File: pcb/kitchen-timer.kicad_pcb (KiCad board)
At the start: 2 copper layers, 41 x 33 mm, 23 parts, among them IC1 ArduinoProMini, J1 EX, J2 3.3V, J3 RT, J4 Conn_01x03, J5 Conn_01x03, J6 LCD, Q1 BC337, Q2 BC327, Q3 BC337, Q4 BC327, Q5 BC337

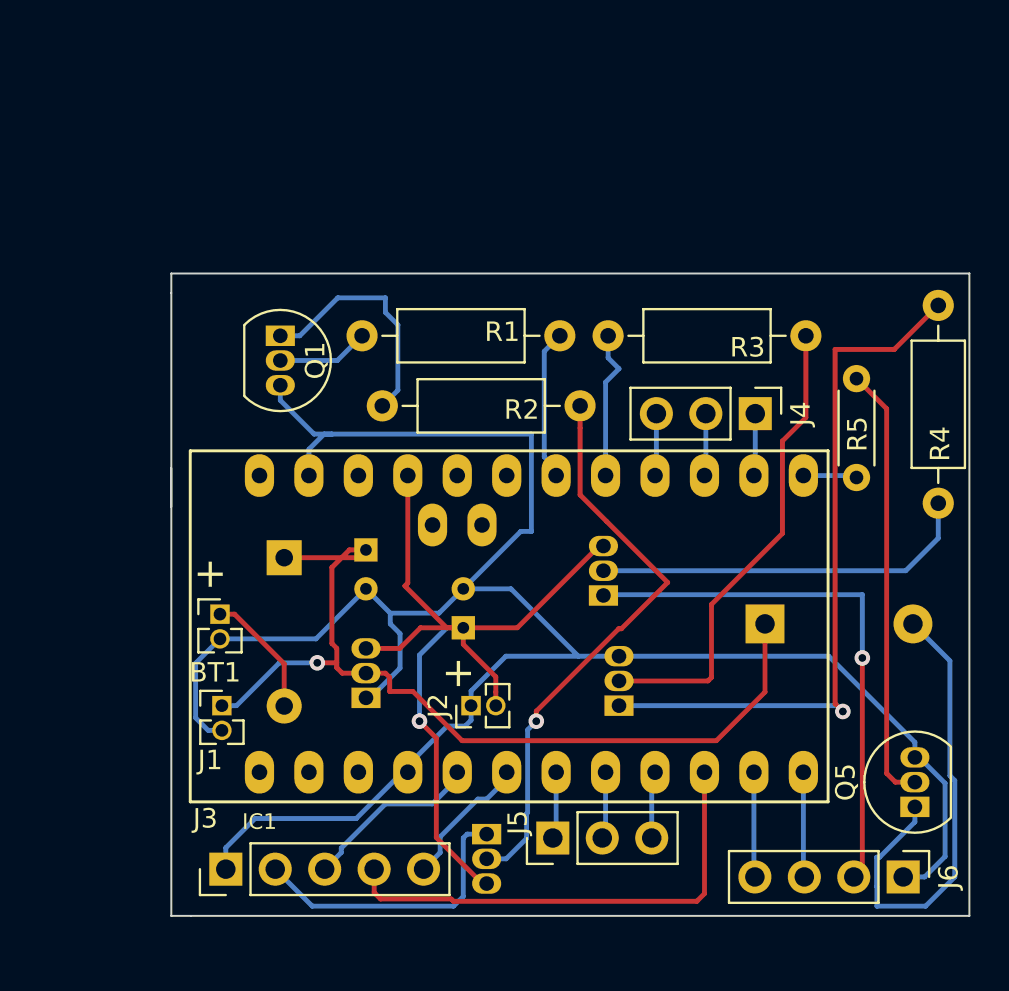
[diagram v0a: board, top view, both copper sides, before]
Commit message: added gnd plane on back
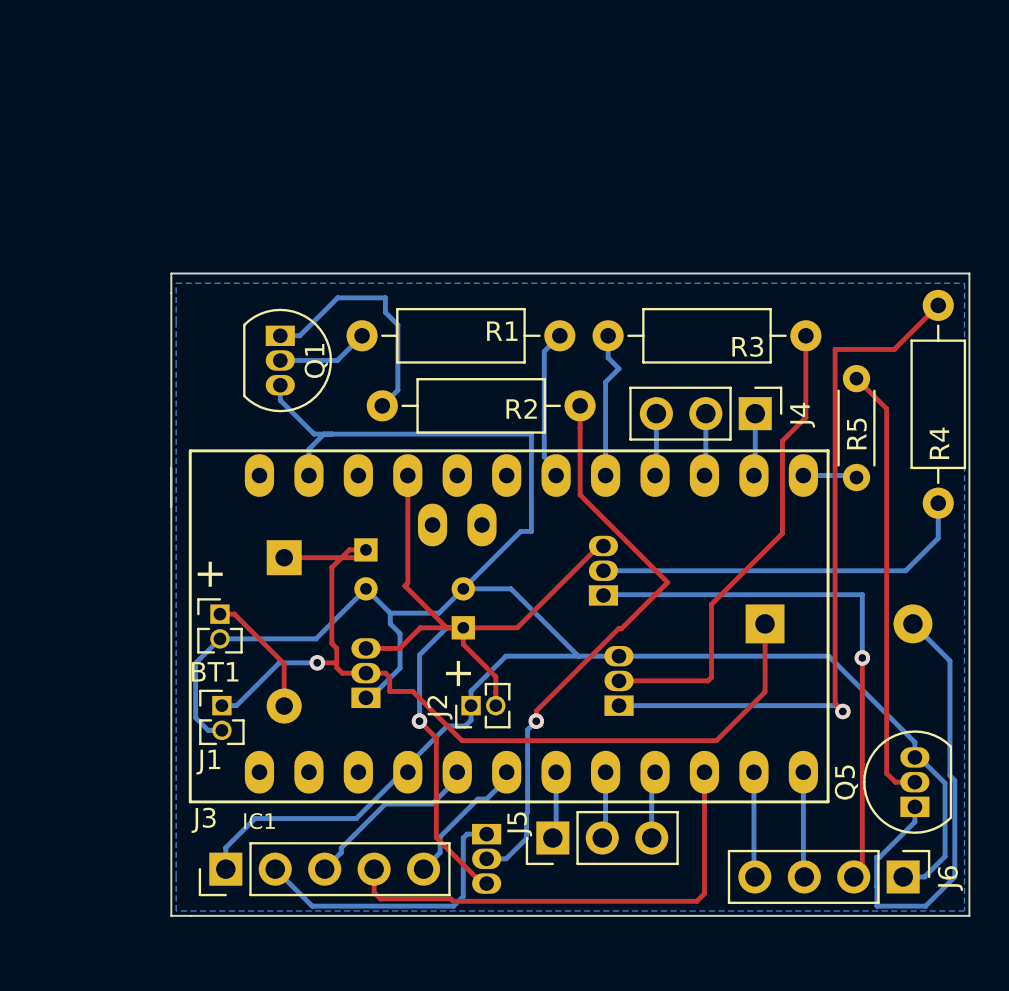
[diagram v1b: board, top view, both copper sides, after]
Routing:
- added copper zone on B.Cu, net -BATT
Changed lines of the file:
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@@
     (pad_drill 0.6)
     (pad_to_mask_clearance 0)
+    (solder_mask_min_width 0.25)
     (aux_axis_origin 0 0)
     (visible_elements FFFFFF7F)
@@
       (outputformat 1)
       (mirror false)
-      (drillshape 1)
+      (drillshape 0)
       (scaleselection 1)
-      (outputdirectory ""))
+      (outputdirectory "/tmp/"))
   )
   (net 0 "")
@@
   (segment (start 149.75 78.95) (end 148.2 77.4) (width 0.25) (layer F.Cu) (net 37))
   (segment (start 149.75 97.68) (end 149.75 78.95) (width 0.25) (layer F.Cu) (net 37))
+  (zone (net 1) (net_name -BATT) (layer B.Cu) (hatch edge 0.508)
+    (connect_pads (clearance 0.508))
+    (min_thickness 0.254)
+    (fill yes (arc_segments 16) (thermal_gap 0.508) (thermal_bridge_width 0.508))
+    (polygon
+      (pts
+        (xy 113.25 72.5) (xy 153.75 72.5) (xy 153.75 104.75) (xy 113.25 104.75) (xy 113.25 103)
+        (xy 113.25 76.75) (xy 113.25 74.5)
+      )
+    )
+  )
 )

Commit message: add pcb
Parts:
- removed BT1: 9V, Connector_PinHeader_1.27mm:PinHeader_1x02_P1.27mm_Vertical
- removed D1: D, Diode_THT:D_A-405_P7.62mm_Horizontal
- removed IC1: ArduinoProMini, arduino:pro_mini
- removed J6: LCD, Connector_PinHeader_2.54mm:PinHeader_1x04_P2.54mm_Vertical
- removed L1: HT7333-A, Package_TO_SOT_THT:TO-92_Inline
- removed Q4: BC327, Package_TO_SOT_THT:TO-92_Inline
- removed Q5: BC337, Package_TO_SOT_THT:TO-92_Inline
- added C3: 100nf, Capacitor_SMD:C_0805_2012Metric_Pad1.15x1.40mm_HandSolder, F.Cu at (109.2, 82.2)
- added U1: ATmega328-PU, Package_DIP:DIP-28_W7.62mm, F.Cu at (111.8, 65.8)
- added Y1: 32khz, Crystal:Crystal_DS15_D1.5mm_L5.0mm_Vertical, F.Cu at (108.0, 86.2)
- BZ1: footprint Buzzer_Beeper:Buzzer_12x9.5RM7.6 -> Connector_PinHeader_2.00mm:PinHeader_1x02_P2.00mm_Vertical; moved to F.Cu
- C1: moved to F.Cu
- C2: value 10uF -> 100nf; footprint Capacitor_THT:CP_Radial_D4.0mm_P2.00mm -> Capacitor_SMD:C_0805_2012Metric_Pad1.15x1.40mm_HandSolder
- J1: value EX -> USB_Breakout IN; footprint Connector_PinHeader_1.27mm:PinHeader_1x02_P1.27mm_Vertical -> Connector_PinHeader_2.00mm:PinHeader_1x02_P2.00mm_Vertical
- J2: value 3.3V -> SW2; footprint Connector_PinHeader_1.27mm:PinHeader_1x02_P1.27mm_Vertical -> Connector_PinHeader_2.00mm:PinHeader_1x02_P2.00mm_Vertical
- J4: value Conn_01x03 -> LCD; footprint Connector_PinHeader_2.54mm:PinHeader_1x03_P2.54mm_Vertical -> Connector_PinHeader_2.54mm:PinHeader_1x04_P2.54mm_Vertical
- J5: value Conn_01x03 -> LED1; footprint Connector_PinHeader_2.54mm:PinHeader_1x03_P2.54mm_Vertical -> Connector_PinHeader_2.00mm:PinHeader_1x02_P2.00mm_Vertical
- Q2: value BC327 -> BC337; moved to F.Cu
- Q3: value BC337 -> BC327; moved to F.Cu
- R1: value 2.6k -> 10k; footprint Resistor_THT:R_Axial_DIN0207_L6.3mm_D2.5mm_P10.16mm_Horizontal -> Resistor_SMD:R_0805_2012Metric_Pad1.15x1.40mm_HandSolder; moved to B.Cu
- R2, R3, R4: footprint Resistor_THT:R_Axial_DIN0207_L6.3mm_D2.5mm_P10.16mm_Horizontal -> Resistor_SMD:R_0805_2012Metric_Pad1.15x1.40mm_HandSolder; moved to B.Cu
- R5: value 2.6k -> 220; footprint Resistor_THT:R_Axial_DIN0204_L3.6mm_D1.6mm_P5.08mm_Horizontal -> Resistor_THT:R_Axial_DIN0207_L6.3mm_D2.5mm_P10.16mm_Horizontal; moved to B.Cu
- moved J5 45.6 mm to (109.0, 62.0)
- moved J3 36.1 mm to (108.2, 67.2), turned to 0 degrees
- moved BZ1 35.8 mm to (108.2, 96.0)
- moved Q1 30.8 mm to (109.0, 104.5), turned to 90 degrees
- moved R4 27.4 mm to (125.2, 87.2)
- moved J4 26.0 mm to (122.8, 95.5), turned to 0 degrees
- moved R5 24.8 mm to (124.0, 72.0), turned to 90 degrees
- moved R2 24.8 mm to (115.5, 95.2), turned to 90 degrees
- moved R3 20.8 mm to (125.5, 80.5), turned to 90 degrees
- moved J2 19.5 mm to (124.0, 75.2), turned to 0 degrees
- moved C1 19.2 mm to (114.2, 103.2), turned to 180 degrees
- moved Q2 18.6 mm to (123.0, 83.2)
- moved C2 14.7 mm to (115.5, 82.5), turned to 270 degrees
- moved Q3 13.8 mm to (123.0, 89.5), turned to 270 degrees
- moved R1 10.3 mm to (115.8, 67.8), turned to 90 degrees
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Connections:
- BZ1 pad 1: Net-(BZ1-Pad1) -> +3V3
- C1 pad 1: Net-(BZ1-Pad1) -> +3V3
- C1 pad 2: -BATT -> GND
- C2 pad 2: -BATT -> GND
- J1 pad 1: Net-(BZ1-Pad1) -> +3V3
- J1 pad 2: -BATT -> GND
- J2 pad 1: -BATT -> Net-(J2-Pad1)
- J2 pad 2: +3V3 -> GND
- J3 pad 1: -BATT -> GND
- J3 pad 2: Net-(J3-Pad2) -> +3V3
- J4 pad 1: Net-(IC1-Pad14) -> GND
- J4 pad 2: Net-(IC1-Pad15) -> Net-(J4-Pad2)
- J4 pad 3: Net-(IC1-Pad16) -> LCD_DIO
- J5 pad 1: Net-(IC1-Pad7) -> GND
- J5 pad 2: Net-(IC1-Pad8) -> Net-(J5-Pad2)
- Q1 pad 1: Net-(Q1-Pad1) -> Net-(BZ1-Pad2)
- Q1 pad 3: -BATT -> GND
- Q2 pad 1: Net-(J3-Pad2) -> Net-(Q2-Pad1)
- Q2 pad 3: +3V3 -> GND
- Q3 pad 1: Net-(Q3-Pad1) -> Net-(J4-Pad2)
- Q3 pad 3: -BATT -> +3V3
- R1 pad 1: Net-(Q1-Pad2) -> +3V3
- R1 pad 2: ENABLE_RT -> Net-(R1-Pad2)
- R2 pad 1: Net-(Q2-Pad2) -> Net-(Q1-Pad2)
- R2 pad 2: Net-(Q1-Pad1) -> Net-(R2-Pad2)
- R3 pad 1: Net-(Q3-Pad2) -> Net-(Q2-Pad2)
- R4 pad 1: Net-(Q4-Pad2) -> Net-(Q3-Pad2)
- R4 pad 2: Net-(Q3-Pad1) -> Net-(Q2-Pad1)
- R5 pad 2: BUZZER -> Net-(J5-Pad2)
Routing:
- net GND: track 0.00 -> 114.9 mm, vias 0 -> 4
- net -BATT: track 113.2 -> 0.00 mm
- net Net-(BZ1-Pad1): track 47.1 -> 0.00 mm, vias 1 -> 0
- net Net-(Q3-Pad1): track 36.6 -> 0.00 mm, vias 1 -> 0
- net +3V3: track 44.8 -> 73.8 mm
- net Net-(J6-Pad2): track 28.0 -> 0.00 mm, vias 1 -> 0
- net Net-(Q2-Pad2): track 29.7 -> 5.31 mm
- net Net-(Q3-Pad2): track 24.4 -> 4.29 mm
- net Net-(Q4-Pad2): track 19.7 -> 0.00 mm
- net Net-(R5-Pad1): track 22.6 -> 5.20 mm
- net Net-(J3-Pad2): track 14.9 -> 0.00 mm
- net Net-(BZ1-Pad2): track 24.5 -> 10.1 mm
- net Net-(J5-Pad2): track 0.00 -> 13.1 mm
- net Net-(Q1-Pad1): track 12.4 -> 0.00 mm
- net Net-(Q1-Pad2): track 4.73 -> 15.9 mm
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- added copper zone on B.Cu, net GND
- removed copper zone on B.Cu, net -BATT
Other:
- board size 41 x 33 mm -> 20.5 x 46.2 mm
